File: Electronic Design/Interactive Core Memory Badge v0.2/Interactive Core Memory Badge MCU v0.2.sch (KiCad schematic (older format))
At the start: 35 parts, among them SW2 SW_Reed, U2 Teensy-LC, U3 LM393, U4 A3214ELHLT-T

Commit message: Adding discrete OR gate
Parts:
- removed U?: 74AHCT1G32, symbol 74xGxx:74AHCT1G32
- added Q? (x2): MMBT4401LT1G, digikey-footprints:SOT-23-3, symbol Digikey-Transistors:MMBT4401LT1G
- added R?: 10k, Resistor_SMD:R_0805_2012Metric, symbol Device:R
- renumbered C2 to C?, C1 to C?, H1 to H?, H2 to H?, R37 to R?, R38 to R?, R40 to R?, R39 to R?, R30 to R?, R33 to R?, R31 to R?, R34 to R?, R32 to R?, R35 to R?, R36 to R?, R41 to R?, R29 to R?, R28 to R?, R42 to R?, SW2 to SW?, TP14 to TP?, TP15 to TP?, TP8 to TP?, TP9 to TP?, TP10 to TP?, TP11 to TP?, TP17 to TP?, TP12 to TP?, TP13 to TP?, TP16 to TP?, TP7 to TP?, U2 to U?, U3 to U?, U4 to U?
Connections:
- net +3V3: now also R?.1
- net I2C_CLOCK: no longer R?.2
- net I2C_DATA: no longer R?.2
- net at U?.7: now also R?.2
- net at U3.1: now also R?.2
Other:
- moved on the sheet: R?

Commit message: Updated drive transistors, switch/diode, OR gate, layout
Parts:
- added C1, C3: 0.1uF, Capacitor_SMD:C_0805_2012Metric, symbol Device:CP1_Small
- added C2, C4: 10uF, Capacitor_SMD:C_0805_2012Metric, symbol Device:CP1_Small
- added C6: 1000uF, Capacitor_SMD:CP_Elec_8x10, symbol Device:CP1_Small
- added R38, R39, R40: 10k, Resistor_SMD:R_0805_2012Metric, symbol Device:R
- added R46: 300, Resistor_SMD:R_0805_2012Metric, symbol Device:R
- added TP12: SENSE_OUT_A, TestPoint:TestPoint_Keystone_5000-5004_Miniature, symbol Connector:TestPoint
- added TP13: SENSE_OUT_B, TestPoint:TestPoint_Keystone_5000-5004_Miniature, symbol Connector:TestPoint
- Q22, Q23: renamed from Q?; footprint digikey-footprints:SOT-23-3 -> Digikey:SOT-23-3
- R31, R34: renamed from R?; value 22 -> 11
- gave numbers to parts that had none: 33
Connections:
- net +3V3: now also Q22.3 (C), Q23.3 (C), C1.1, C2.1
- net +VSW: now also C3.1, C4.1, C6.1
- net -BATT: now also C3.2, C4.2, C6.2
- net GNDD: now also C1.2, C2.2, R40.2
- net I2C_CLOCK: now also R45.2
- net I2C_DATA: now also R44.2
- net LED_MATRIX: now also R46.1; no longer H2.2 (+)
- net SENSE_PULSE: now also Q22.2 (E), Q23.2 (E), R40.1
- net at R37.2, U3.7: now also R39.2, TP13.1
- net at R36.2, U3.1: now also R38.2, TP12.1
- net at Q22.1 (B): now also R38.1
- net at Q23.1 (B): now also R39.1
- new net: H2.2 (+), R46.2
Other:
- note added: "DNI"
- note added: "NOTES:\nv0.2 represents improvements learned from producing v0.1, along witih some additional best\npractices (decoupling caps, series LED matrix signal resistor and large power filter cap).\nv0.2 was not produced, but it should work well."
- moved on the sheet: H1, H2, Q22, Q23, R37, R44, R45, TP14, TP19, U3B, U3C

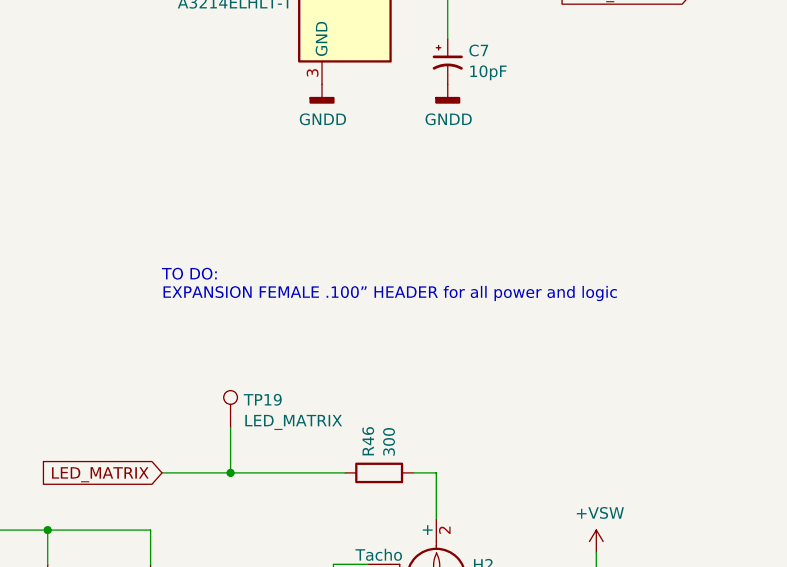
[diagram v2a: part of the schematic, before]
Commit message: Tweaks to V0.2 schematic and layout from notes.
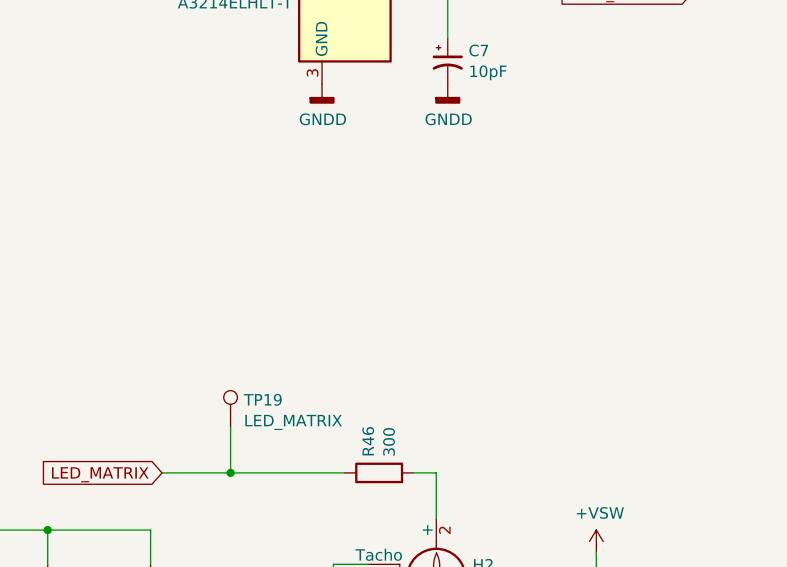
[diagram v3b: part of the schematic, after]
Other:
- note removed: "TO DO:\nEXPANSION FEMALE .100” HEADER for all power and logic"
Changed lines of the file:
@@
 	1800 3550 1000 3550
 Connection ~ 1000 3550
-Text Notes 8700 4250 0    50   ~ 0
-TO DO:\nEXPANSION FEMALE .100” HEADER for all power and logic
 $Comp
 L Comparator:LM393 U?
